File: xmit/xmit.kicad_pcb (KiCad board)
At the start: 4 copper layers, 59.8 x 36.7 mm, 31 parts, among them U1 74LVC1G66, U2 74LVC1G66, U3 74LVC1G66, U4 74LVC1G66, U5 74LVC1G66, U6 74LVC1G66

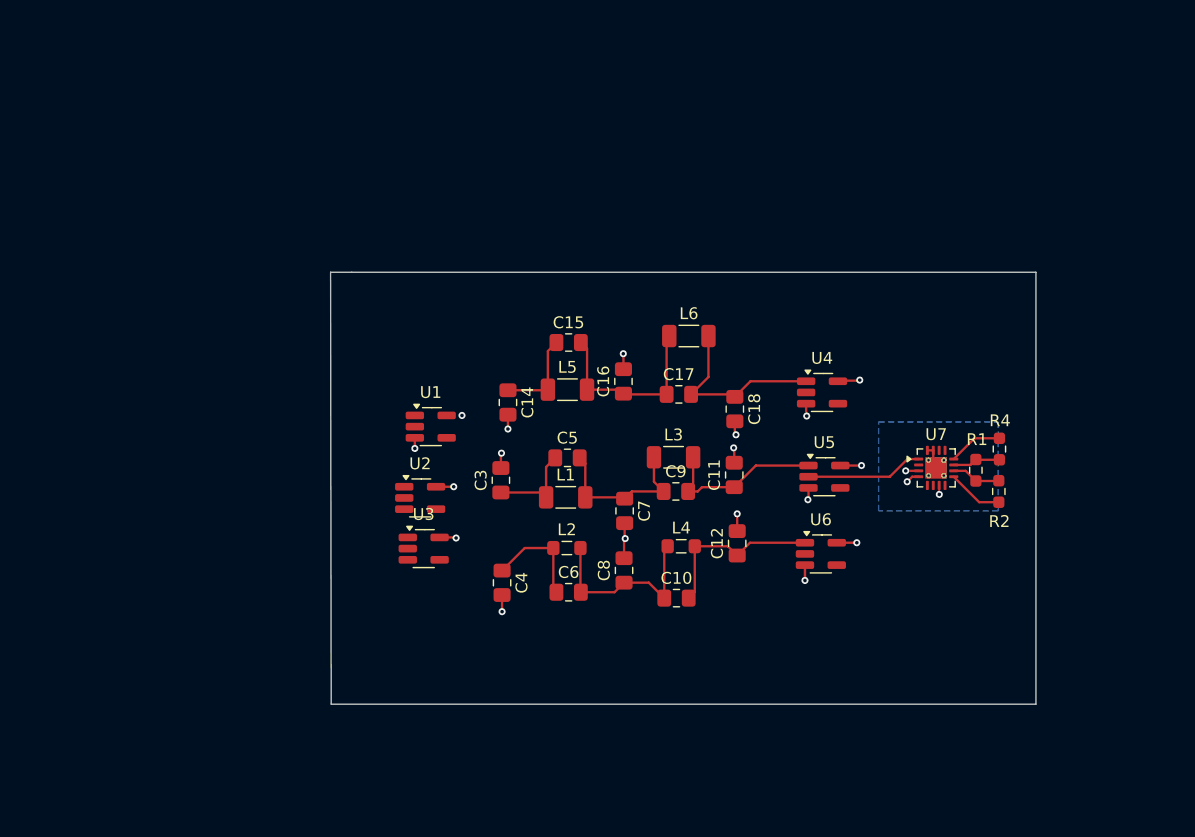
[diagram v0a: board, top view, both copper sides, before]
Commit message: WIP commit, but the circuit is nearly done and PCB is beginning for form.
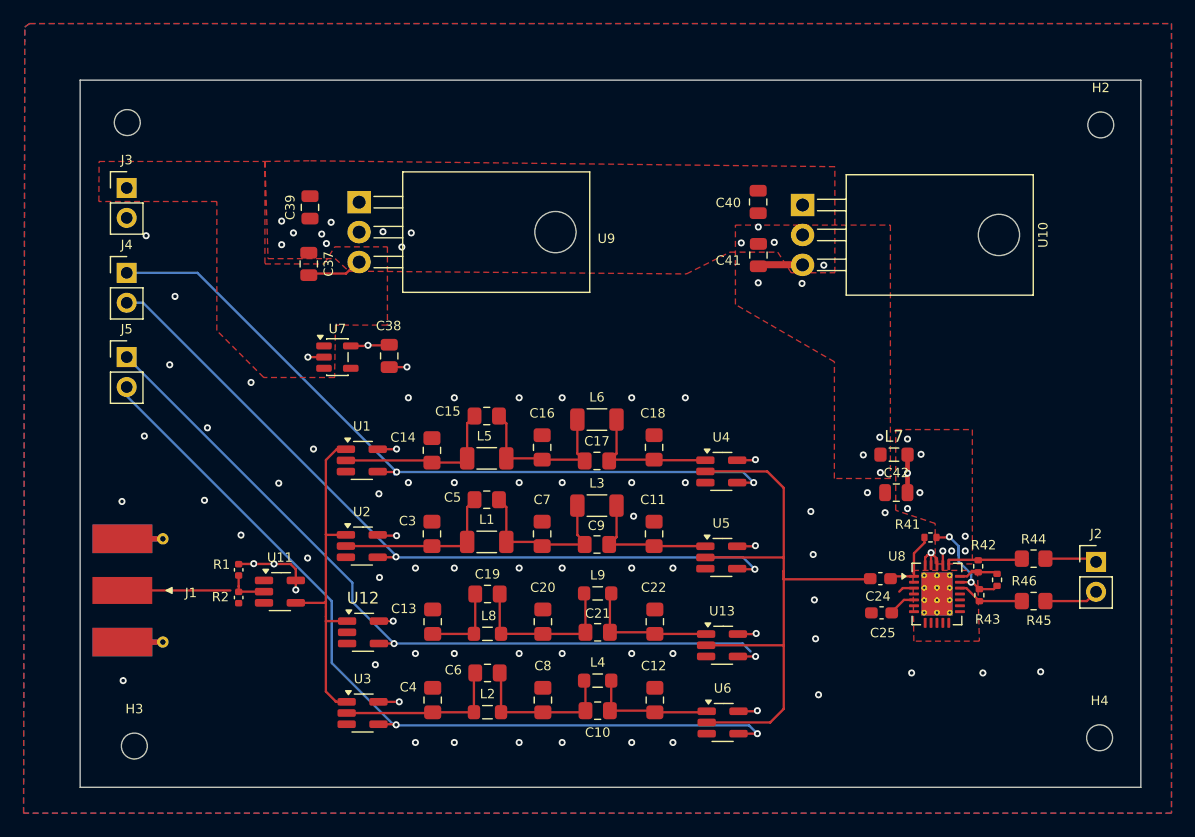
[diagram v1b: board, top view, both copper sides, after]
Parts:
- removed R4: 1.24k, Resistor_SMD:R_0603_1608Metric_Pad0.98x0.95mm_HandSolder
- added C13: 50p, Capacitor_SMD:C_0805_2012Metric_Pad1.18x1.45mm_HandSolder, F.Cu at (159.9, 86.0)
- added C19: 3.9p, Capacitor_SMD:C_0805_2012Metric_Pad1.18x1.45mm_HandSolder, F.Cu at (164.6, 83.6)
- added C20: 81p, Capacitor_SMD:C_0805_2012Metric_Pad1.18x1.45mm_HandSolder, F.Cu at (169.3, 86.0)
- added C21: 9p, Capacitor_SMD:C_0805_2012Metric_Pad1.18x1.45mm_HandSolder, F.Cu at (173.9, 86.8)
- added C22: 50p, Capacitor_SMD:C_0805_2012Metric_Pad1.18x1.45mm_HandSolder, F.Cu at (178.8, 86.0)
- added C24: 100n, Capacitor_SMD:C_0603_1608Metric_Pad1.08x0.95mm_HandSolder, F.Cu at (197.9, 82.3)
- added C25: 100n, Capacitor_SMD:C_0603_1608Metric_Pad1.08x0.95mm_HandSolder, F.Cu at (198.0, 85.2)
- added C37: 1u, Capacitor_SMD:C_0805_2012Metric, F.Cu at (149.4, 55.6)
- added C38: 1u, Capacitor_SMD:C_0805_2012Metric, F.Cu at (156.2, 63.4)
- added C39: 0.33µ, Capacitor_SMD:C_0805_2012Metric, F.Cu at (149.5, 50.8)
- added C40: 0.33µ, Capacitor_SMD:C_0805_2012Metric, F.Cu at (187.5, 50.3)
- added C41: 1µ, Capacitor_SMD:C_0805_2012Metric, F.Cu at (187.6, 54.8)
- added C42: 1µ, Capacitor_SMD:C_0805_2012Metric, F.Cu at (199.2, 75.0)
- added H1: MountingHole, MountingHole:MountingHole_2.2mm_M2, F.Cu at (134.0, 43.6)
- added H2: MountingHole, MountingHole:MountingHole_2.2mm_M2, F.Cu at (216.6, 43.8)
- added H3: MountingHole, MountingHole:MountingHole_2.2mm_M2, F.Cu at (134.6, 96.5)
- added H4: MountingHole, MountingHole:MountingHole_2.2mm_M2, F.Cu at (216.5, 95.8)
- added J1: Conn_Coaxial, Connector_Coaxial:SMA_Molex_73251-1153_EdgeMount_Horizontal, F.Cu at (135.3, 83.3)
- added J2: Conn_01x02, Connector_PinHeader_2.54mm:PinHeader_1x02_P2.54mm_Vertical, F.Cu at (216.2, 80.9)
- added J3: Conn_01x02, Connector_PinHeader_2.54mm:PinHeader_1x02_P2.54mm_Vertical, F.Cu at (133.9, 49.1)
- added J4: Conn_01x02, Connector_PinHeader_2.54mm:PinHeader_1x02_P2.54mm_Vertical, F.Cu at (133.9, 56.4)
- added J5: Conn_01x02, Connector_PinHeader_2.54mm:PinHeader_1x02_P2.54mm_Vertical, F.Cu at (133.9, 63.5)
- added L7: 800µ, Inductor_SMD:L_0805_2012Metric_Pad1.05x1.20mm_HandSolder, F.Cu at (199.1, 71.8)
- added L8: 800n, Inductor_SMD:L_0805_2012Metric_Pad1.05x1.20mm_HandSolder, F.Cu at (164.6, 87.0)
- added L9: 800n, Inductor_SMD:L_0805_2012Metric_Pad1.05x1.20mm_HandSolder, F.Cu at (173.9, 83.5)
- added R41: 1.24k, Resistor_SMD:R_0402_1005Metric, F.Cu at (202.2, 78.8)
- added R42: 1.24k, Resistor_SMD:R_0402_1005Metric, F.Cu at (206.2, 81.2)
- added R43: 1.24k, Resistor_SMD:R_0402_1005Metric, F.Cu at (206.3, 83.7)
- added R44: 2.5, Resistor_SMD:R_0805_2012Metric_Pad1.20x1.40mm_HandSolder, F.Cu at (210.9, 80.6)
- added R45: 2.5, Resistor_SMD:R_0805_2012Metric_Pad1.20x1.40mm_HandSolder, F.Cu at (210.9, 84.2)
- added R46: 237, Resistor_SMD:R_0402_1005Metric, F.Cu at (207.8, 82.4)
- added U10: L7812, Package_TO_SOT_THT:TO-220-3_Horizontal_TabDown, F.Cu at (191.3, 50.6)
- added U11: SN74LVC1G04DBV, Package_TO_SOT_SMD:SOT-23-5_HandSoldering, F.Cu at (146.9, 83.4)
- added U12: 74LVC1G66, Package_TO_SOT_SMD:SOT-23-5_HandSoldering, F.Cu at (154.0, 86.8)
- added U13: 74LVC1G66, Package_TO_SOT_SMD:SOT-23-5_HandSoldering, F.Cu at (184.5, 88.0)
- added U8: ~, Package_DFN_QFN:QFN-24-1EP_4x5mm_P0.5mm_EP2.65x3.65mm_ThermalVias, F.Cu at (202.7, 83.6)
- added U9: L7805, Package_TO_SOT_THT:TO-220-3_Horizontal_TabDown, F.Cu at (153.7, 50.4)
- R1: value 274 -> 200; footprint Resistor_SMD:R_0603_1608Metric_Pad0.98x0.95mm_HandSolder -> Capacitor_SMD:C_0402_1005Metric
- R2: value 1.24k -> 200; footprint Resistor_SMD:R_0603_1608Metric_Pad0.98x0.95mm_HandSolder -> Capacitor_SMD:C_0402_1005Metric
- U7: value ~ -> TPS7A20xxxDBV; footprint Package_DFN_QFN:VQFN-16-1EP_3x3mm_P0.5mm_EP1.8x1.8mm_ThermalVias -> Package_TO_SOT_SMD:SOT-23-5
- moved R2 65.1 mm to (143.4, 83.9), turned to -90 degrees
- moved R1 63.1 mm to (143.4, 81.5), turned to -90 degrees
- moved U7 51.7 mm to (151.8, 63.5)
- moved U6 16.6 mm to (184.5, 94.5)
- moved L2 15.5 mm to (164.6, 93.6)
- moved C12 15.0 mm to (178.8, 92.6)
- moved U3 14.9 mm to (154.0, 93.7)
- moved L4 13.4 mm to (173.9, 91.0)
- moved C8 13.0 mm to (169.3, 92.6)
- moved C10 11.7 mm to (173.9, 93.5)
- moved C4 11.6 mm to (159.9, 92.6), turned to 90 degrees
- moved U5 11.1 mm to (184.4, 80.5)
- moved U4 10.9 mm to (184.4, 73.2)
- moved L6 10.5 mm to (173.8, 68.8)
- moved C6 9.71 mm to (164.6, 90.3)
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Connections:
- net /transmit filters/RF_in renamed Net-(U1-Pad1)
- net /transmit filters/band_10 renamed band.10m
- net /transmit filters/band_20 renamed band.20m
- net /transmit filters/band_30 renamed band.30m
- R1 pad 1: Net-(U7-D2_IN-) -> +3V3
- R1 pad 2: Net-(U7-D1_IN-) -> RF_in
- R2 pad 1: /transmit filters/RF- -> RF_in
- R2 pad 2: Net-(U7-D2_IN-) -> GND
- U1 pad 5: unconnected-(U1B-VCC-Pad5) -> +3V3
- U4 pad 2: Net-(U7-D1_IN+) -> rf_drive
- U5 pad 2: Net-(U7-D1_IN+) -> rf_drive
- U6 pad 2: Net-(U7-D1_IN+) -> rf_drive
- U7 pad 1: Net-(U7-D1_IN+) -> +5V
- U7 pad 2: Net-(U7-D2_IN+) -> GND
- U7 pad 3: GND -> +5V
- U7 pad 4: +3V3 -> unconnected-(U7-NC-Pad4)
- U7 pad 5: Net-(U7-D2_IN+) -> +3V3
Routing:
- net band.10m: track 0.00 -> 72.3 mm, vias 0 -> 2
- net band.20m: track 0.00 -> 65.9 mm, vias 0 -> 2
- net band.15m: track 0.00 -> 65.5 mm, vias 0 -> 1
- net band.30m: track 0.00 -> 64.5 mm, vias 0 -> 2
- net rf_drive: track 0.00 -> 54.3 mm
- net Net-(U1-Pad1): track 0.00 -> 30.0 mm
- net Net-(C19-Pad2): track 0.00 -> 14.0 mm
- net RF_in: track 0.00 -> 12.7 mm
- net GND: track 20.3 -> 7.71 mm, vias 14 -> 72
- net Net-(C21-Pad2): track 0.00 -> 11.6 mm
- net +3V3: track 9.50 -> 21.0 mm, vias 7 -> 11
- net Net-(U8-D2_IN-): track 0.00 -> 10.7 mm, vias 0 -> 2
- net Net-(U7-D1_IN+): track 9.97 -> 0.00 mm
- net Net-(U8-D1_OUT): track 0.00 -> 7.18 mm
- net Net-(C13-Pad1): track 0.00 -> 6.93 mm
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- added copper zone on F.Cu, net +12V
- added copper zone on In2.Cu, net +12V
- added copper zone on F.Cu, net +5V
- added copper zone on In2.Cu, net +5V
- added copper zone on F.Cu, net /Power/+20V
- added copper zone on F.Cu, net /Power/raw12V
- added copper zone on In2.Cu, net /Power/raw12V
- added copper zone on F.Cu, net GND
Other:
- board size 59.8 x 36.7 mm -> 90 x 60 mm

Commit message: Updated filters and improved amp
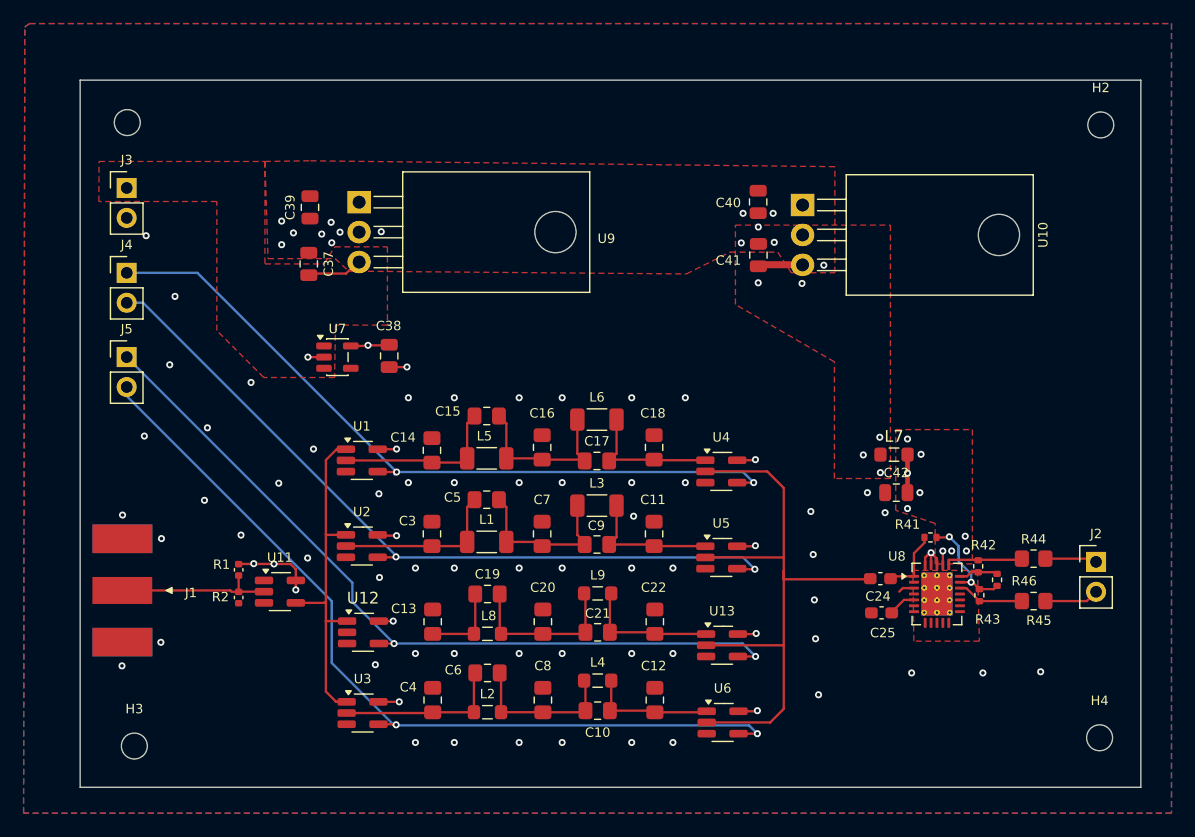
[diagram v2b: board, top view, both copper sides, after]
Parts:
- C10: value 9p -> 5.6p
- C12, C4: value 50p -> 33p
- C6: value 3.9p -> 2.2p
- C8: value 81p -> 72p
- L2, L4: value 800n -> 56n
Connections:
- J5 pad 1: band.15m -> band.10m
- J5 pad 2: band.10m -> band.2m
- U12 pad 3: (no net) -> GND
- U12 pad 4: band.15m -> band.10m
- U12 pad 5: (no net) -> +3V3
- U13 pad 3: (no net) -> GND
- U13 pad 4: /Filters/band.14m -> band.10m
- U13 pad 5: (no net) -> +3V3
- U3 pad 4: band.10m -> band.2m
- U6 pad 4: band.10m -> band.2m
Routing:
- net band.2m: track 0.00 -> 72.3 mm, vias 0 -> 2
- net band.15m: track 65.5 -> 0.00 mm, vias 1 -> 0
- net band.10m: track 72.3 -> 67.7 mm
- net /Filters/band.14m: track 1.60 -> 0.00 mm, vias 1 -> 0
- net (no net): track 1.25 -> 0.00 mm, vias 1 -> 0
- net +3V3: track 21.0 -> 22.2 mm, vias 11 -> 12
- net Net-(C5-Pad2): track 14.3 -> 13.3 mm
- net Net-(C14-Pad1): track 14.4 -> 13.6 mm
- net RF_in: track 12.7 -> 13.4 mm
- net band.30m: track 64.5 -> 63.9 mm
- net Net-(C10-Pad1): track 13.2 -> 12.7 mm
- net Net-(C19-Pad2): track 14.0 -> 13.5 mm
- net Net-(C3-Pad1): track 14.3 -> 13.8 mm
- net Net-(C17-Pad2): track 12.0 -> 11.5 mm
- net GND: vias 72 -> 75

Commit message: Another WIP on transmitter layout. Should be pretty close.
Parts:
- removed J3: Conn_01x02, Connector_PinHeader_2.54mm:PinHeader_1x02_P2.54mm_Vertical
- added J6: Conn_01x02, Connector:terminal_block_02, F.Cu at (200.5, 63.2)
- C24, C25: footprint Capacitor_SMD:C_0603_1608Metric_Pad1.08x0.95mm_HandSolder -> Capacitor_SMD:C_0805_2012Metric_Pad1.18x1.45mm_HandSolder
- J1: footprint Connector_Coaxial:SMA_Molex_73251-1153_EdgeMount_Horizontal -> Connector_Coaxial:SMA_Samtec_SMA-J-P-H-ST-EM1_EdgeMount
- J2, J4, J5: footprint Connector_PinHeader_2.54mm:PinHeader_1x02_P2.54mm_Vertical -> Connector:terminal_block_02
- L1, L3, L5, L6: footprint Inductor_SMD:L_1206_3216Metric_Pad1.22x1.90mm_HandSolder -> Inductor_SMD:L_0805_2012Metric_Pad1.05x1.20mm_HandSolder
- R1, R2: footprint Capacitor_SMD:C_0402_1005Metric -> Resistor_SMD:R_0805_2012Metric_Pad1.20x1.40mm_HandSolder
- U9: value L7805 -> TLV760; footprint Package_TO_SOT_THT:TO-220-3_Horizontal_TabDown -> Package_TO_SOT_SMD:TSOT-23
- moved U10 22.2 mm to (183.8, 71.5), turned to 0 degrees
- moved C41 20.8 mm to (199.9, 71.6), turned to 180 degrees
- moved C40 20.3 mm to (196.9, 68.3), turned to 180 degrees
- moved H2 18.4 mm to (201.6, 54.5)
- moved H4 16.7 mm to (201.5, 88.5)
- moved R44 15.5 mm to (195.4, 80.7)
- moved R45 15.5 mm to (195.4, 84.3)
- moved J2 15.1 mm to (201.2, 82.4), turned to 90 degrees
- moved R43 14.9 mm to (191.4, 83.8)
- moved R46 14.9 mm to (192.9, 82.5)
- moved C25 14.9 mm to (183.1, 85.3)
- moved R41 14.9 mm to (187.2, 78.9)
- moved R42 14.9 mm to (191.3, 81.3)
- moved U8 14.9 mm to (187.8, 83.7)
- moved C24 14.9 mm to (183.0, 82.2)
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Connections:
- J2 pad 1: out+ -> out-
- J2 pad 2: out- -> out+
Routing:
- net band.30m: track 63.9 -> 48.1 mm
- net band.10m: track 67.7 -> 52.0 mm
- net band.20m: track 65.9 -> 51.2 mm
- net band.2m: track 72.3 -> 61.8 mm
- net Net-(C13-Pad1): track 6.76 -> 15.1 mm
- net rf_drive: track 54.2 -> 49.1 mm
- net +5V: track 4.73 -> 0.00 mm, vias 0 -> 3
- net GND: track 7.71 -> 3.46 mm, vias 75 -> 125
- net /Power/raw12V: track 3.73 -> 0.00 mm, vias 6 -> 4
- net +12V: track 4.42 -> 1.20 mm, vias 9 -> 5
- net Net-(U1-Pad1): track 30.0 -> 33.1 mm
- net Net-(C5-Pad2): track 13.3 -> 16.1 mm
- net Net-(C10-Pad1): track 12.7 -> 15.3 mm
- net Net-(C15-Pad2): track 14.1 -> 16.6 mm
- net Net-(C19-Pad2): track 13.5 -> 15.6 mm
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- added copper zone on In2.Cu, net /Power/+20V
- added copper zone on In2.Cu, net GND
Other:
- board size 90 x 60 mm -> 75 x 41 mm
- board text added: "+15-20V"
- board text added: "10m"
- board text added: "20m"
- board text added: "2m"
- board text added: "30m"
- board text added: "Band select"
- board text added: "GND"
- board text added: "RF Amplifier"
- board text added: "RF In"
- board text added: "RF Out"
